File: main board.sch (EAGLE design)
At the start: 60 parts, among them SW1 BOOT_SW, SW2 RST_SW, X1 MINI-USB, Y1 SMDRESONATOR

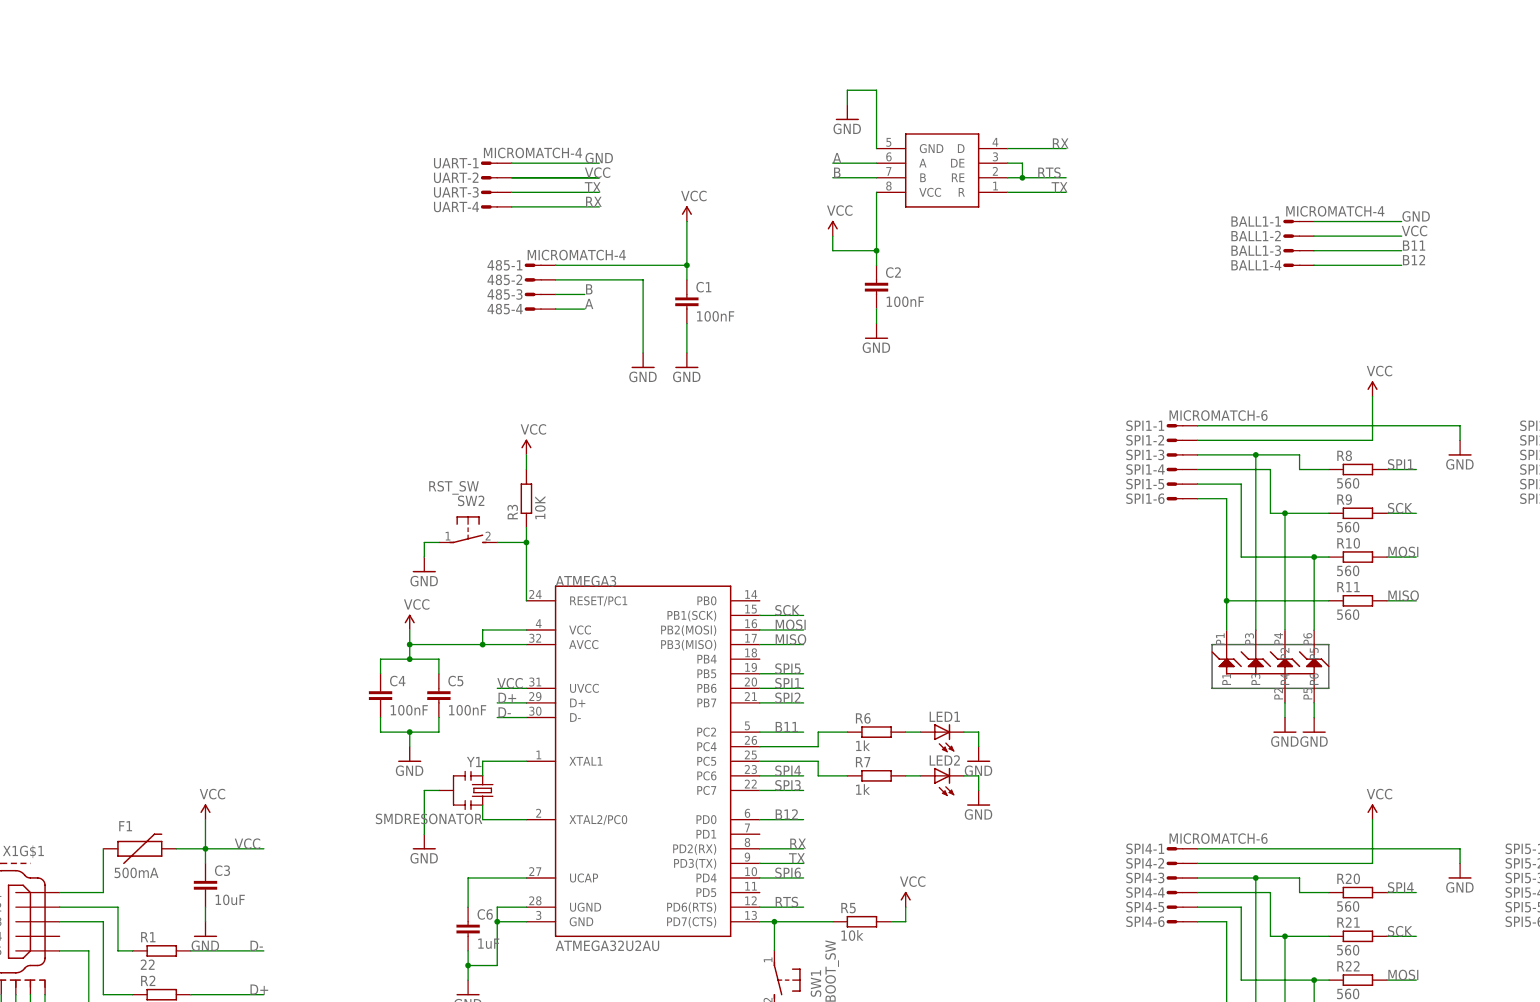
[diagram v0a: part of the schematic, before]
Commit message: All pins rooted into micromatches.
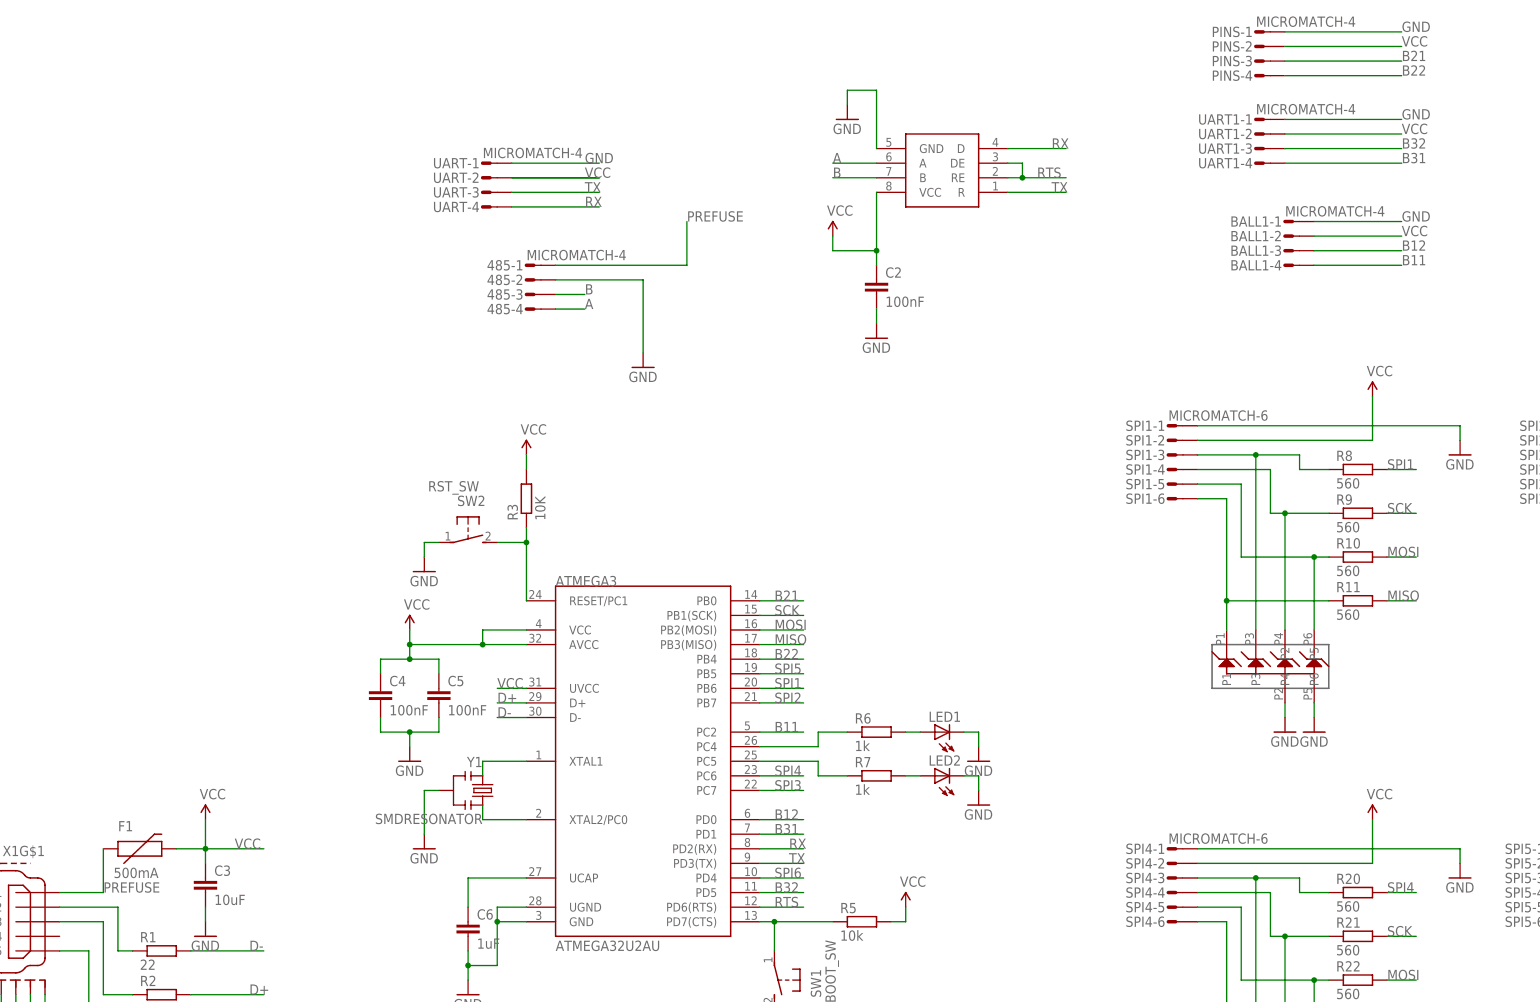
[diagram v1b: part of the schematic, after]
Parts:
- removed C1: 100nF, rcl:C-EUC0603
- added PINS, UART1: MICROMATCH-4, con-amp-micromatch:MICROMATCH-4
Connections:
- removed net N$4: F1.1, X1G$1.1
- new net B21: ATMEGA3.PB0, PINS-3.S
- new net B22: ATMEGA3.PB4, PINS-4.S
- new net B31: ATMEGA3.PD1, UART1-4.S
- new net B32: ATMEGA3.PD5, UART1-3.S
- new net PREFUSE: 485-1.S, F1.1, X1G$1.1
- net B11: now also BALL1-4.S; no longer BALL1-3.S
- net B12: now also BALL1-3.S; no longer BALL1-4.S
- net GND: now also PINS-1.S, UART1-1.S; no longer C1.2
- net VCC: now also PINS-2.S, UART1-2.S; no longer 485-1.S, C1.1
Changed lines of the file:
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@@
 <part name="GND29" library="supply1" deviceset="GND" device=""/>
 <part name="GND30" library="supply1" deviceset="GND" device=""/>
-<part name="GND31" library="supply1" deviceset="GND" device=""/>
-<part name="SUPPLY12" library="SparkFun-Aesthetics" deviceset="VCC" device=""/>
 <part name="GND2" library="supply1" deviceset="GND" device=""/>
 <part name="ATMEGA3" library="SparkFun" deviceset="ATMEGA8U2" device="AU" value="ATMEGA32U2AU"/>
-<part name="C1" library="rcl" deviceset="C-EU" device="C0603" value="100nF"/>
 <part name="C2" library="rcl" deviceset="C-EU" device="C0603" value="100nF"/>
 <part name="BALL1" library="con-amp-micromatch" deviceset="MICROMATCH-4" device=""/>
 <part name="485" library="con-amp-micromatch" deviceset="MICROMATCH-4" device=""/>
+<part name="UART1" library="con-amp-micromatch" deviceset="MICROMATCH-4" device=""/>
+<part name="PINS" library="con-amp-micromatch" deviceset="MICROMATCH-4" device=""/>
 </parts>
 <sheets>
@@
 <instance part="GND29" gate="1" x="119.38" y="121.92"/>
 <instance part="GND30" gate="1" x="83.82" y="78.74"/>
-<instance part="GND31" gate="1" x="91.44" y="78.74"/>
-<instance part="SUPPLY12" gate="G$1" x="91.44" y="104.14"/>
 <instance part="GND2" gate="1" x="-12.7" y="-48.26"/>
 <instance part="ATMEGA3" gate="G$1" x="83.82" y="10.16"/>
-<instance part="C1" gate="G$1" x="91.44" y="91.44"/>
 <instance part="C2" gate="G$1" x="124.46" y="93.98"/>
 <instance part="BALL1" gate="-1" x="195.58" y="104.14"/>
@@
 <instance part="485" gate="-3" x="63.5" y="91.44"/>
 <instance part="485" gate="-4" x="63.5" y="88.9"/>
+<instance part="UART1" gate="-1" x="190.5" y="121.92"/>
+<instance part="UART1" gate="-2" x="190.5" y="119.38"/>
+<instance part="UART1" gate="-3" x="190.5" y="116.84"/>
+<instance part="UART1" gate="-4" x="190.5" y="114.3"/>
+<instance part="PINS" gate="-1" x="190.5" y="137.16"/>
+<instance part="PINS" gate="-2" x="190.5" y="134.62"/>
+<instance part="PINS" gate="-3" x="190.5" y="132.08"/>
+<instance part="PINS" gate="-4" x="190.5" y="129.54"/>
 </instances>
 <busses>
@@
 <wire x1="119.38" y1="127" x2="119.38" y2="124.46" width="0.1524" layer="91"/>
 <pinref part="GND29" gate="1" pin="GND"/>
-</segment>
-<segment>
-<wire x1="91.44" y1="86.36" x2="91.44" y2="81.28" width="0.1524" layer="91"/>
-<pinref part="GND31" gate="1" pin="GND"/>
-<pinref part="C1" gate="G$1" pin="2"/>
 </segment>
 <segment>
@@
 <wire x1="83.82" y1="93.98" x2="68.58" y2="93.98" width="0.1524" layer="91"/>
 </segment>
+<segment>
+<pinref part="PINS" gate="-1" pin="S"/>
+<wire x1="195.58" y1="137.16" x2="215.9" y2="137.16" width="0.1524" layer="91"/>
+<label x="215.9" y="137.16" size="1.778" layer="95"/>
+</segment>
+<segment>
+<pinref part="UART1" gate="-1" pin="S"/>
+<wire x1="195.58" y1="121.92" x2="215.9" y2="121.92" width="0.1524" layer="91"/>
+<label x="215.9" y="121.92" size="1.778" layer="95"/>
+</segment>
 </net>
 <net name="N$2" class="0">
@@
 </segment>
 </net>
-<net name="N$4" class="0">
+<net name="PREFUSE" class="0">
 <segment>
 <pinref part="X1" gate="G$1" pin="1"/>
@@
 <wire x1="-17.78" y1="-12.7" x2="-10.16" y2="-12.7" width="0.1524" layer="91"/>
 <wire x1="-10.16" y1="-12.7" x2="-10.16" y2="-5.08" width="0.1524" layer="91"/>
+<label x="-10.16" y="-12.7" size="1.778" layer="95"/>
+</segment>
+<segment>
+<wire x1="91.44" y1="96.52" x2="91.44" y2="104.14" width="0.1524" layer="91"/>
+<wire x1="68.58" y1="96.52" x2="91.44" y2="96.52" width="0.1524" layer="91"/>
+<pinref part="485" gate="-1" pin="S"/>
+<label x="91.44" y="104.14" size="1.778" layer="95"/>
 </segment>
 </net>
@@
 </segment>
 <segment>
-<pinref part="SUPPLY12" gate="G$1" pin="VCC"/>
-<wire x1="91.44" y1="93.98" x2="91.44" y2="96.52" width="0.1524" layer="91"/>
-<wire x1="91.44" y1="96.52" x2="91.44" y2="104.14" width="0.1524" layer="91"/>
-<junction x="91.44" y="96.52"/>
-<pinref part="C1" gate="G$1" pin="1"/>
-<wire x1="68.58" y1="96.52" x2="91.44" y2="96.52" width="0.1524" layer="91"/>
-<pinref part="485" gate="-1" pin="S"/>
-</segment>
-<segment>
 <pinref part="BALL1" gate="-2" pin="S"/>
 <wire x1="200.66" y1="101.6" x2="215.9" y2="101.6" width="0.1524" layer="91"/>
 <label x="215.9" y="101.6" size="1.778" layer="95"/>
+</segment>
+<segment>
+<pinref part="PINS" gate="-2" pin="S"/>
+<wire x1="195.58" y1="134.62" x2="215.9" y2="134.62" width="0.1524" layer="91"/>
+<label x="215.9" y="134.62" size="1.778" layer="95"/>
+</segment>
+<segment>
+<pinref part="UART1" gate="-2" pin="S"/>
+<wire x1="195.58" y1="119.38" x2="215.9" y2="119.38" width="0.1524" layer="91"/>
+<label x="215.9" y="119.38" size="1.778" layer="95"/>
 </segment>
 </net>
@@
 <net name="B11" class="0">
 <segment>
+<pinref part="ATMEGA3" gate="G$1" pin="PC2"/>
+<wire x1="104.14" y1="15.24" x2="111.76" y2="15.24" width="0.1524" layer="91"/>
+<label x="106.68" y="15.24" size="1.778" layer="95"/>
+</segment>
+<segment>
+<pinref part="BALL1" gate="-4" pin="S"/>
+<wire x1="200.66" y1="96.52" x2="215.9" y2="96.52" width="0.1524" layer="91"/>
+<label x="215.9" y="96.52" size="1.778" layer="95"/>
+</segment>
+</net>
+<net name="B12" class="0">
+<segment>
+<pinref part="ATMEGA3" gate="G$1" pin="PD0"/>
+<wire x1="104.14" y1="0" x2="111.76" y2="0" width="0.1524" layer="91"/>
+<label x="106.68" y="0" size="1.778" layer="95"/>
+</segment>
+<segment>
 <pinref part="BALL1" gate="-3" pin="S"/>
 <wire x1="200.66" y1="99.06" x2="215.9" y2="99.06" width="0.1524" layer="91"/>
 <label x="215.9" y="99.06" size="1.778" layer="95"/>
 </segment>
-<segment>
-<pinref part="ATMEGA3" gate="G$1" pin="PC2"/>
-<wire x1="104.14" y1="15.24" x2="111.76" y2="15.24" width="0.1524" layer="91"/>
-<label x="106.68" y="15.24" size="1.778" layer="95"/>
-</segment>
-</net>
-<net name="B12" class="0">
-<segment>
-<pinref part="BALL1" gate="-4" pin="S"/>
-<wire x1="200.66" y1="96.52" x2="215.9" y2="96.52" width="0.1524" layer="91"/>
-<label x="215.9" y="96.52" size="1.778" layer="95"/>
-</segment>
-<segment>
-<pinref part="ATMEGA3" gate="G$1" pin="PD0"/>
-<wire x1="104.14" y1="0" x2="111.76" y2="0" width="0.1524" layer="91"/>
-<label x="106.68" y="0" size="1.778" layer="95"/>
-</segment>
-</net>
+</net>
+<net name="B32" class="0">
+<segment>
+<pinref part="ATMEGA3" gate="G$1" pin="PD5"/>
+<wire x1="104.14" y1="-12.7" x2="111.76" y2="-12.7" width="0.1524" layer="91"/>
+<label x="106.68" y="-12.7" size="1.778" layer="95"/>
+</segment>
+<segment>
+<pinref part="UART1" gate="-3" pin="S"/>
+<wire x1="195.58" y1="116.84" x2="215.9" y2="116.84" width="0.1524" layer="91"/>
+<label x="215.9" y="116.84" size="1.778" layer="95"/>
+</segment>
+</net>
+<net name="B21" class="0">
+<segment>
+<pinref part="PINS" gate="-3" pin="S"/>
+<wire x1="195.58" y1="132.08" x2="215.9" y2="132.08" width="0.1524" layer="91"/>
+<label x="215.9" y="132.08" size="1.778" layer="95"/>
+</segment>
+<segment>
+<wire x1="104.14" y1="38.1" x2="111.76" y2="38.1" width="0.1524" layer="91"/>
+<label x="106.68" y="38.1" size="1.778" layer="95"/>
+<pinref part="ATMEGA3" gate="G$1" pin="PB0"/>
+</segment>
+</net>
+<net name="B22" class="0">
+<segment>
+<pinref part="PINS" gate="-4" pin="S"/>
+<wire x1="195.58" y1="129.54" x2="215.9" y2="129.54" width="0.1524" layer="91"/>
+<label x="215.9" y="129.54" size="1.778" layer="95"/>
+</segment>
+<segment>
+<pinref part="ATMEGA3" gate="G$1" pin="PB4"/>
+<wire x1="104.14" y1="27.94" x2="111.76" y2="27.94" width="0.1524" layer="91"/>
+<label x="106.68" y="27.94" size="1.778" layer="95"/>
+</segment>
+</net>
+<net name="B31" class="0">
+<segment>
+<pinref part="ATMEGA3" gate="G$1" pin="PD1"/>
+<wire x1="104.14" y1="-2.54" x2="111.76" y2="-2.54" width="0.1524" layer="91"/>
+<label x="106.68" y="-2.54" size="1.778" layer="95"/>
+</segment>
+<segment>
+<pinref part="UART1" gate="-4" pin="S"/>
+<wire x1="195.58" y1="114.3" x2="215.9" y2="114.3" width="0.1524" layer="91"/>
+<label x="215.9" y="114.3" size="1.778" layer="95"/>
+</segment>
+</net>

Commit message: Rotated one micromatch.
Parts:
- renumbered UART1 to PINS2
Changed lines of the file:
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@@
 <part name="BALL1" library="con-amp-micromatch" deviceset="MICROMATCH-4" device=""/>
 <part name="485" library="con-amp-micromatch" deviceset="MICROMATCH-4" device=""/>
-<part name="UART1" library="con-amp-micromatch" deviceset="MICROMATCH-4" device=""/>
+<part name="PINS2" library="con-amp-micromatch" deviceset="MICROMATCH-4" device=""/>
 <part name="PINS" library="con-amp-micromatch" deviceset="MICROMATCH-4" device=""/>
 </parts>
@@
 <instance part="485" gate="-3" x="63.5" y="91.44"/>
 <instance part="485" gate="-4" x="63.5" y="88.9"/>
-<instance part="UART1" gate="-1" x="190.5" y="121.92"/>
-<instance part="UART1" gate="-2" x="190.5" y="119.38"/>
-<instance part="UART1" gate="-3" x="190.5" y="116.84"/>
-<instance part="UART1" gate="-4" x="190.5" y="114.3"/>
+<instance part="PINS2" gate="-1" x="190.5" y="121.92"/>
+<instance part="PINS2" gate="-2" x="190.5" y="119.38"/>
+<instance part="PINS2" gate="-3" x="190.5" y="116.84"/>
+<instance part="PINS2" gate="-4" x="190.5" y="114.3"/>
 <instance part="PINS" gate="-1" x="190.5" y="137.16"/>
 <instance part="PINS" gate="-2" x="190.5" y="134.62"/>
@@
 </segment>
 <segment>
-<pinref part="UART1" gate="-1" pin="S"/>
+<pinref part="PINS2" gate="-1" pin="S"/>
 <wire x1="195.58" y1="121.92" x2="215.9" y2="121.92" width="0.1524" layer="91"/>
 <label x="215.9" y="121.92" size="1.778" layer="95"/>
@@
 </segment>
 <segment>
-<pinref part="UART1" gate="-2" pin="S"/>
+<pinref part="PINS2" gate="-2" pin="S"/>
 <wire x1="195.58" y1="119.38" x2="215.9" y2="119.38" width="0.1524" layer="91"/>
 <label x="215.9" y="119.38" size="1.778" layer="95"/>
@@
 </segment>
 <segment>
-<pinref part="UART1" gate="-3" pin="S"/>
+<pinref part="PINS2" gate="-3" pin="S"/>
 <wire x1="195.58" y1="116.84" x2="215.9" y2="116.84" width="0.1524" layer="91"/>
 <label x="215.9" y="116.84" size="1.778" layer="95"/>
@@
 </segment>
 <segment>
-<pinref part="UART1" gate="-4" pin="S"/>
+<pinref part="PINS2" gate="-4" pin="S"/>
 <wire x1="195.58" y1="114.3" x2="215.9" y2="114.3" width="0.1524" layer="91"/>
 <label x="215.9" y="114.3" size="1.778" layer="95"/>

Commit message: Tweaks to GND plane
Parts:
- added R4: 120, rcl:R-EU_R0603
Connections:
- net A: now also R4.2
- net B: now also R4.1
- net B11: now also PINS-3.S; no longer BALL1-4.S
- net B12: now also PINS-4.S; no longer BALL1-3.S
- net B21: now also BALL1-4.S; no longer PINS-3.S
- net B22: now also BALL1-3.S; no longer PINS-4.S
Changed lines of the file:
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@@
 <part name="PINS2" library="con-amp-micromatch" deviceset="MICROMATCH-4" device=""/>
 <part name="PINS" library="con-amp-micromatch" deviceset="MICROMATCH-4" device=""/>
+<part name="R4" library="rcl" deviceset="R-EU_" device="R0603" value="120"/>
 </parts>
 <sheets>
@@
 <instance part="PINS" gate="-3" x="190.5" y="132.08"/>
 <instance part="PINS" gate="-4" x="190.5" y="129.54"/>
+<instance part="R4" gate="G$1" x="96.52" y="121.92" rot="R90"/>
 </instances>
 <busses>
@@
 <label x="73.66" y="91.44" size="1.778" layer="95"/>
 </segment>
+<segment>
+<pinref part="R4" gate="G$1" pin="1"/>
+<wire x1="96.52" y1="116.84" x2="96.52" y2="114.3" width="0.1524" layer="91"/>
+<wire x1="96.52" y1="114.3" x2="93.98" y2="114.3" width="0.1524" layer="91"/>
+<wire x1="96.52" y1="114.3" x2="99.06" y2="114.3" width="0.1524" layer="91"/>
+<label x="99.06" y="114.3" size="1.778" layer="95"/>
+<junction x="96.52" y="114.3"/>
+</segment>
 </net>
 <net name="A" class="0">
@@
 <label x="73.66" y="88.9" size="1.778" layer="95"/>
 </segment>
+<segment>
+<pinref part="R4" gate="G$1" pin="2"/>
+<wire x1="96.52" y1="127" x2="96.52" y2="129.54" width="0.1524" layer="91"/>
+<wire x1="99.06" y1="129.54" x2="96.52" y2="129.54" width="0.1524" layer="91"/>
+<wire x1="96.52" y1="129.54" x2="93.98" y2="129.54" width="0.1524" layer="91"/>
+<label x="99.06" y="129.54" size="1.778" layer="95"/>
+<junction x="96.52" y="129.54"/>
+</segment>
 </net>
 <net name="B11" class="0">
@@
 </segment>
 <segment>
+<pinref part="PINS" gate="-3" pin="S"/>
+<wire x1="195.58" y1="132.08" x2="215.9" y2="132.08" width="0.1524" layer="91"/>
+<label x="215.9" y="132.08" size="1.778" layer="95"/>
+</segment>
+</net>
+<net name="B12" class="0">
+<segment>
+<pinref part="ATMEGA3" gate="G$1" pin="PD0"/>
+<wire x1="104.14" y1="0" x2="111.76" y2="0" width="0.1524" layer="91"/>
+<label x="106.68" y="0" size="1.778" layer="95"/>
+</segment>
+<segment>
+<pinref part="PINS" gate="-4" pin="S"/>
+<wire x1="195.58" y1="129.54" x2="215.9" y2="129.54" width="0.1524" layer="91"/>
+<label x="215.9" y="129.54" size="1.778" layer="95"/>
+</segment>
+</net>
+<net name="B32" class="0">
+<segment>
+<pinref part="ATMEGA3" gate="G$1" pin="PD5"/>
+<wire x1="104.14" y1="-12.7" x2="111.76" y2="-12.7" width="0.1524" layer="91"/>
+<label x="106.68" y="-12.7" size="1.778" layer="95"/>
+</segment>
+<segment>
+<pinref part="PINS2" gate="-3" pin="S"/>
+<wire x1="195.58" y1="116.84" x2="215.9" y2="116.84" width="0.1524" layer="91"/>
+<label x="215.9" y="116.84" size="1.778" layer="95"/>
+</segment>
+</net>
+<net name="B21" class="0">
+<segment>
+<wire x1="104.14" y1="38.1" x2="111.76" y2="38.1" width="0.1524" layer="91"/>
+<label x="106.68" y="38.1" size="1.778" layer="95"/>
+<pinref part="ATMEGA3" gate="G$1" pin="PB0"/>
+</segment>
+<segment>
 <pinref part="BALL1" gate="-4" pin="S"/>
 <wire x1="200.66" y1="96.52" x2="215.9" y2="96.52" width="0.1524" layer="91"/>
@@
 </segment>
 </net>
-<net name="B12" class="0">
-<segment>
-<pinref part="ATMEGA3" gate="G$1" pin="PD0"/>
-<wire x1="104.14" y1="0" x2="111.76" y2="0" width="0.1524" layer="91"/>
-<label x="106.68" y="0" size="1.778" layer="95"/>
+<net name="B22" class="0">
+<segment>
+<pinref part="ATMEGA3" gate="G$1" pin="PB4"/>
+<wire x1="104.14" y1="27.94" x2="111.76" y2="27.94" width="0.1524" layer="91"/>
+<label x="106.68" y="27.94" size="1.778" layer="95"/>
 </segment>
 <segment>
@@
 </segment>
 </net>
-<net name="B32" class="0">
-<segment>
-<pinref part="ATMEGA3" gate="G$1" pin="PD5"/>
-<wire x1="104.14" y1="-12.7" x2="111.76" y2="-12.7" width="0.1524" layer="91"/>
-<label x="106.68" y="-12.7" size="1.778" layer="95"/>
-</segment>
-<segment>
-<pinref part="PINS2" gate="-3" pin="S"/>
-<wire x1="195.58" y1="116.84" x2="215.9" y2="116.84" width="0.1524" layer="91"/>
-<label x="215.9" y="116.84" size="1.778" layer="95"/>
-</segment>
-</net>
-<net name="B21" class="0">
-<segment>
-<pinref part="PINS" gate="-3" pin="S"/>
-<wire x1="195.58" y1="132.08" x2="215.9" y2="132.08" width="0.1524" layer="91"/>
-<label x="215.9" y="132.08" size="1.778" layer="95"/>
-</segment>
-<segment>
-<wire x1="104.14" y1="38.1" x2="111.76" y2="38.1" width="0.1524" layer="91"/>
-<label x="106.68" y="38.1" size="1.778" layer="95"/>
-<pinref part="ATMEGA3" gate="G$1" pin="PB0"/>
-</segment>
-</net>
-<net name="B22" class="0">
-<segment>
-<pinref part="PINS" gate="-4" pin="S"/>
-<wire x1="195.58" y1="129.54" x2="215.9" y2="129.54" width="0.1524" layer="91"/>
-<label x="215.9" y="129.54" size="1.778" layer="95"/>
-</segment>
-<segment>
-<pinref part="ATMEGA3" gate="G$1" pin="PB4"/>
-<wire x1="104.14" y1="27.94" x2="111.76" y2="27.94" width="0.1524" layer="91"/>
-<label x="106.68" y="27.94" size="1.778" layer="95"/>
-</segment>
-</net>
